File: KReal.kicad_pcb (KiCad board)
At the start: 2 copper layers, 100 x 90 mm, 91 parts, among them J101 USB, J102 3mm, J103 3mm, J104 3mm, J105 3mm, J201 5V Bypass, P101 X AXIS, P102 Y AXIS, P103 Z AXIS, P104 A AXIS, P105 X SW, P106 Y SW, P107 Z SW, P108 A SW, P109 EMO Z SW, P110 PWM, P111 Power, P112 UART, P113 SPI, P201 ICSP, Q101 Q_NPN_BEC, Q102 Q_NPN_BEC, Q201 BSS138, U101 PIC32MX775F, U102 CD4048B, U103 CD4048B, U201 MC34063, U202 AP3417C, U204 MMBZ5226BTS-3.3v, U301 TLP293-4, U302 TLP293-4, U303 TLP293-4, Y201 10.0MHz, Y202 32.768kHz

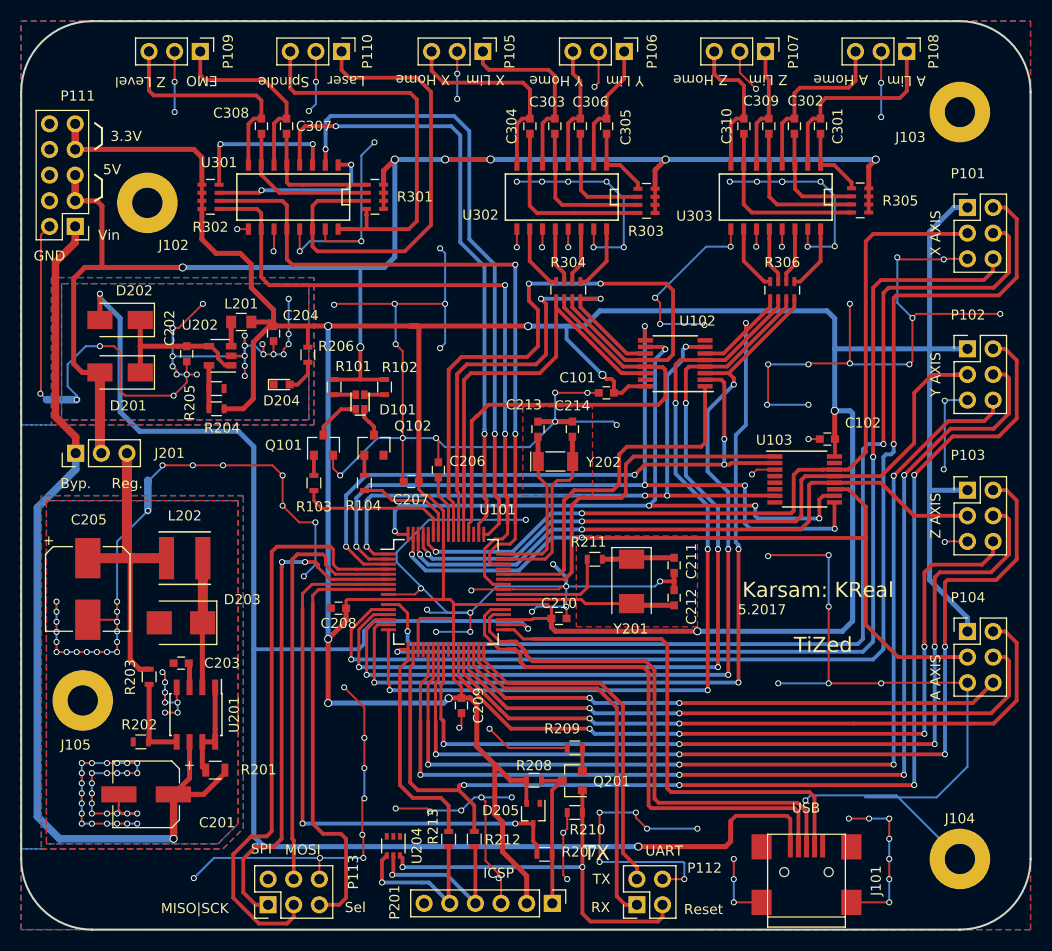
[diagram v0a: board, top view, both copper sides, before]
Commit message: Fixed USB in layout. Fixed LEDs power source.
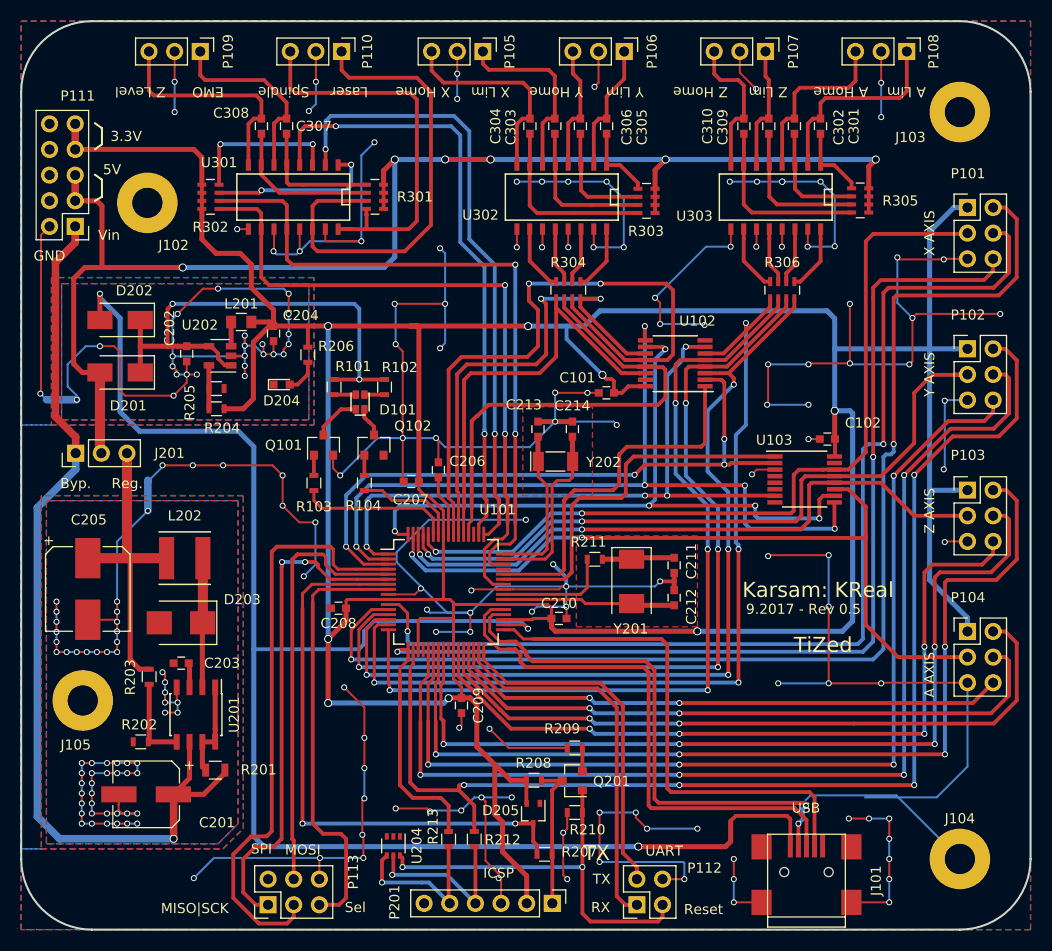
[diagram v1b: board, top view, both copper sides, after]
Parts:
- C210: value 10nF -> 100nF
- Q101, Q102: value Q_NPN_BEC -> MMBT2222A
- Y201: value 10.0MHz -> 20.0MHz
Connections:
- C202 pad 1: Net-(C202-Pad1) -> V_leds
- D201 pad 1: Net-(C202-Pad1) -> V_leds
- D202 pad 1: Net-(C202-Pad1) -> V_leds
- J101 pad 2: D_P -> D_N
- J101 pad 3: D_N -> D_P
- R101 pad 1: +5V -> V_leds
- R102 pad 1: +5V -> V_leds
- U202 pad 1: Net-(C202-Pad1) -> V_leds
- U202 pad 4: Net-(C202-Pad1) -> V_leds
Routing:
- net V_leds: track 0.00 -> 50.4 mm, vias 0 -> 2
- net +5V: track 153.7 -> 137.6 mm, vias 7 -> 6
- net Net-(C202-Pad1): track 15.3 -> 0.00 mm
- net GND: track 753.1 -> 760.2 mm, vias 204 -> 203
- net D_N: track 52.7 -> 53.7 mm, vias 0 -> 2
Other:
- board text added: "9.2017 - Rev 0.5"
- board text removed: "5.2017"
